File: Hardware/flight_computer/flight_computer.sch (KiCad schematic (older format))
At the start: 38 parts, among them J1 Micro_USB, J2 MicroSD_molex, J3 rpi_zero_w, Q1 PMOS_20V_.76A, Q2 PMOS_20V_.76A, U1 FRAM_128K, U2 STM32F427VITx, U3 MCP131T-300E_TT, Y1 Crystal_24MHZ

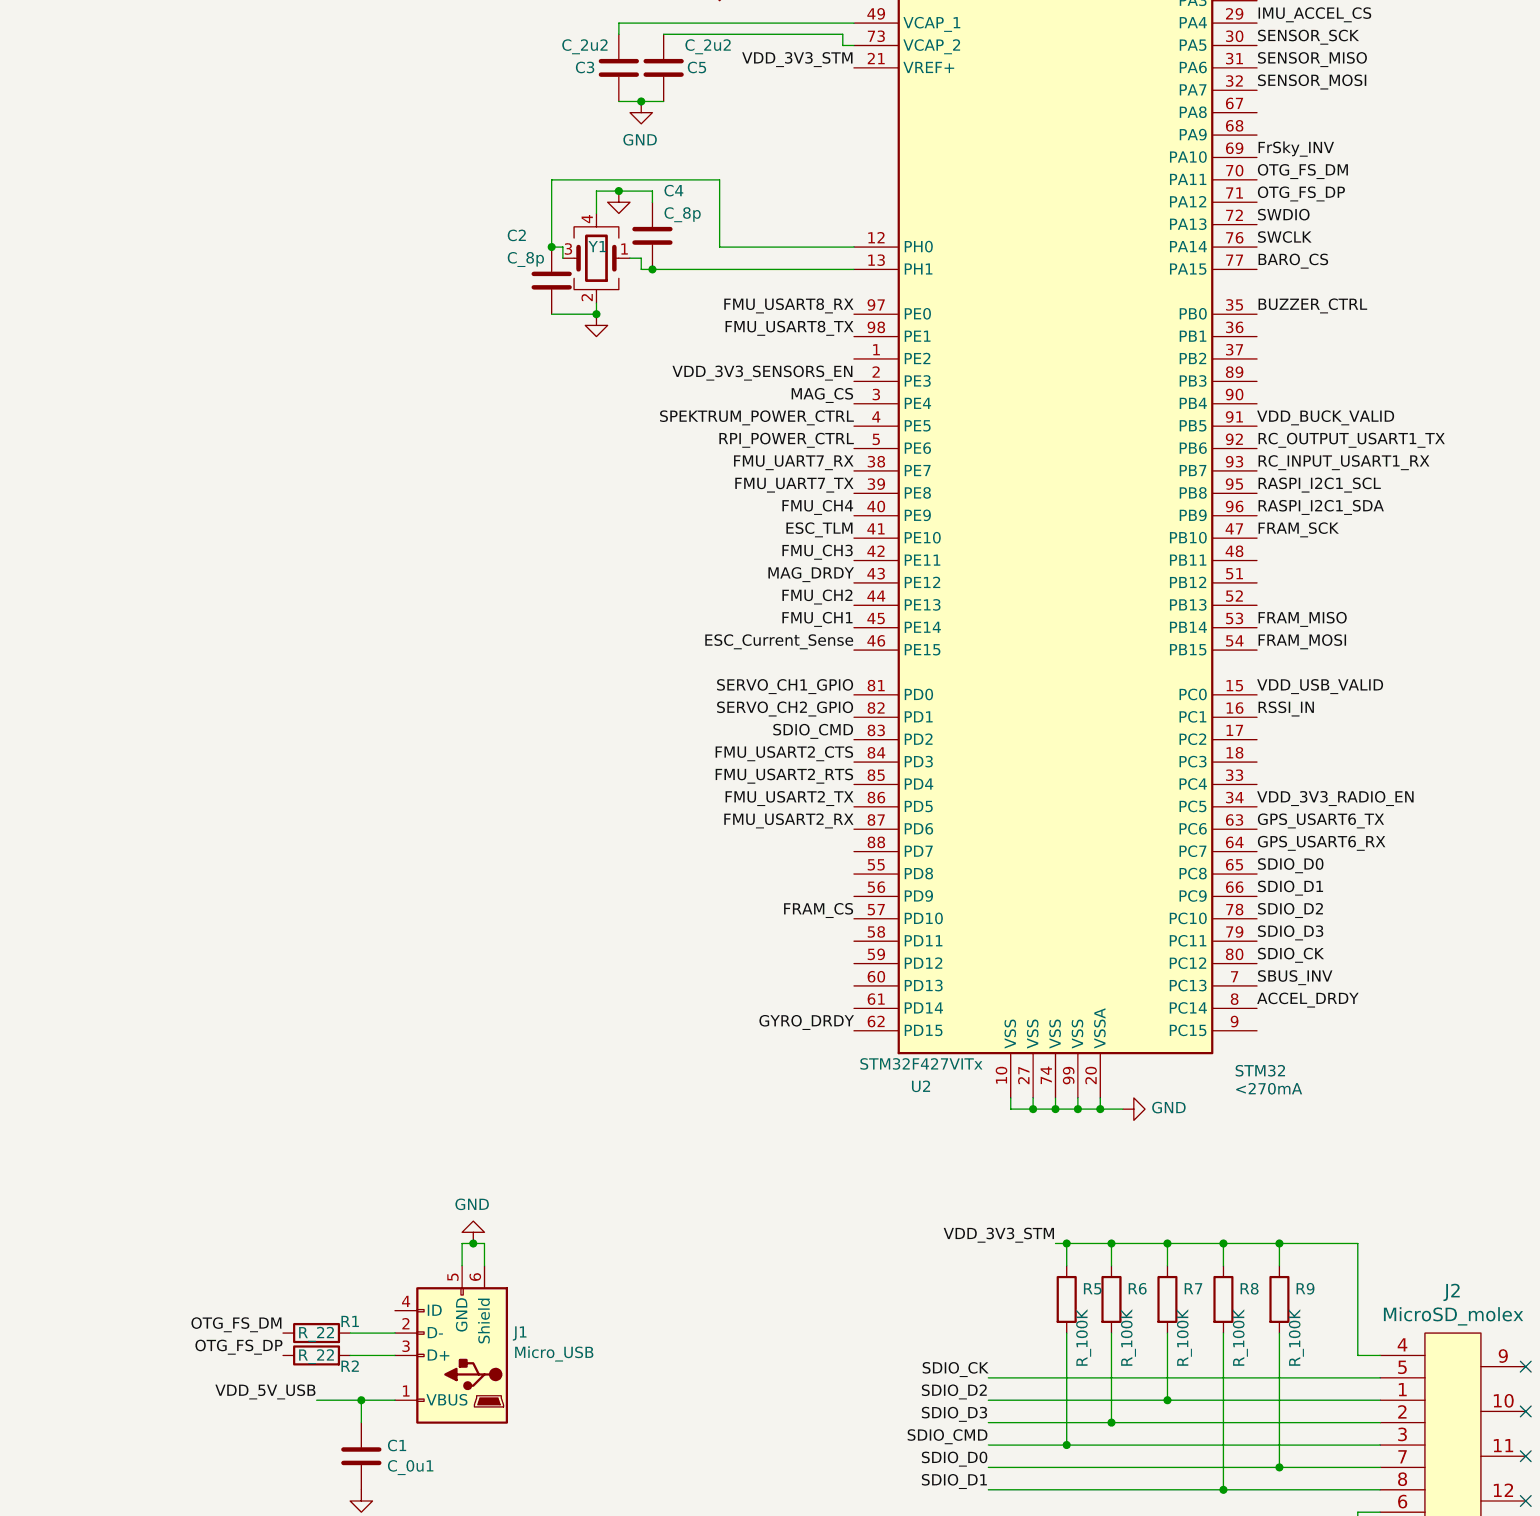
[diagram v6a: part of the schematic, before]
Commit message: started buck layout
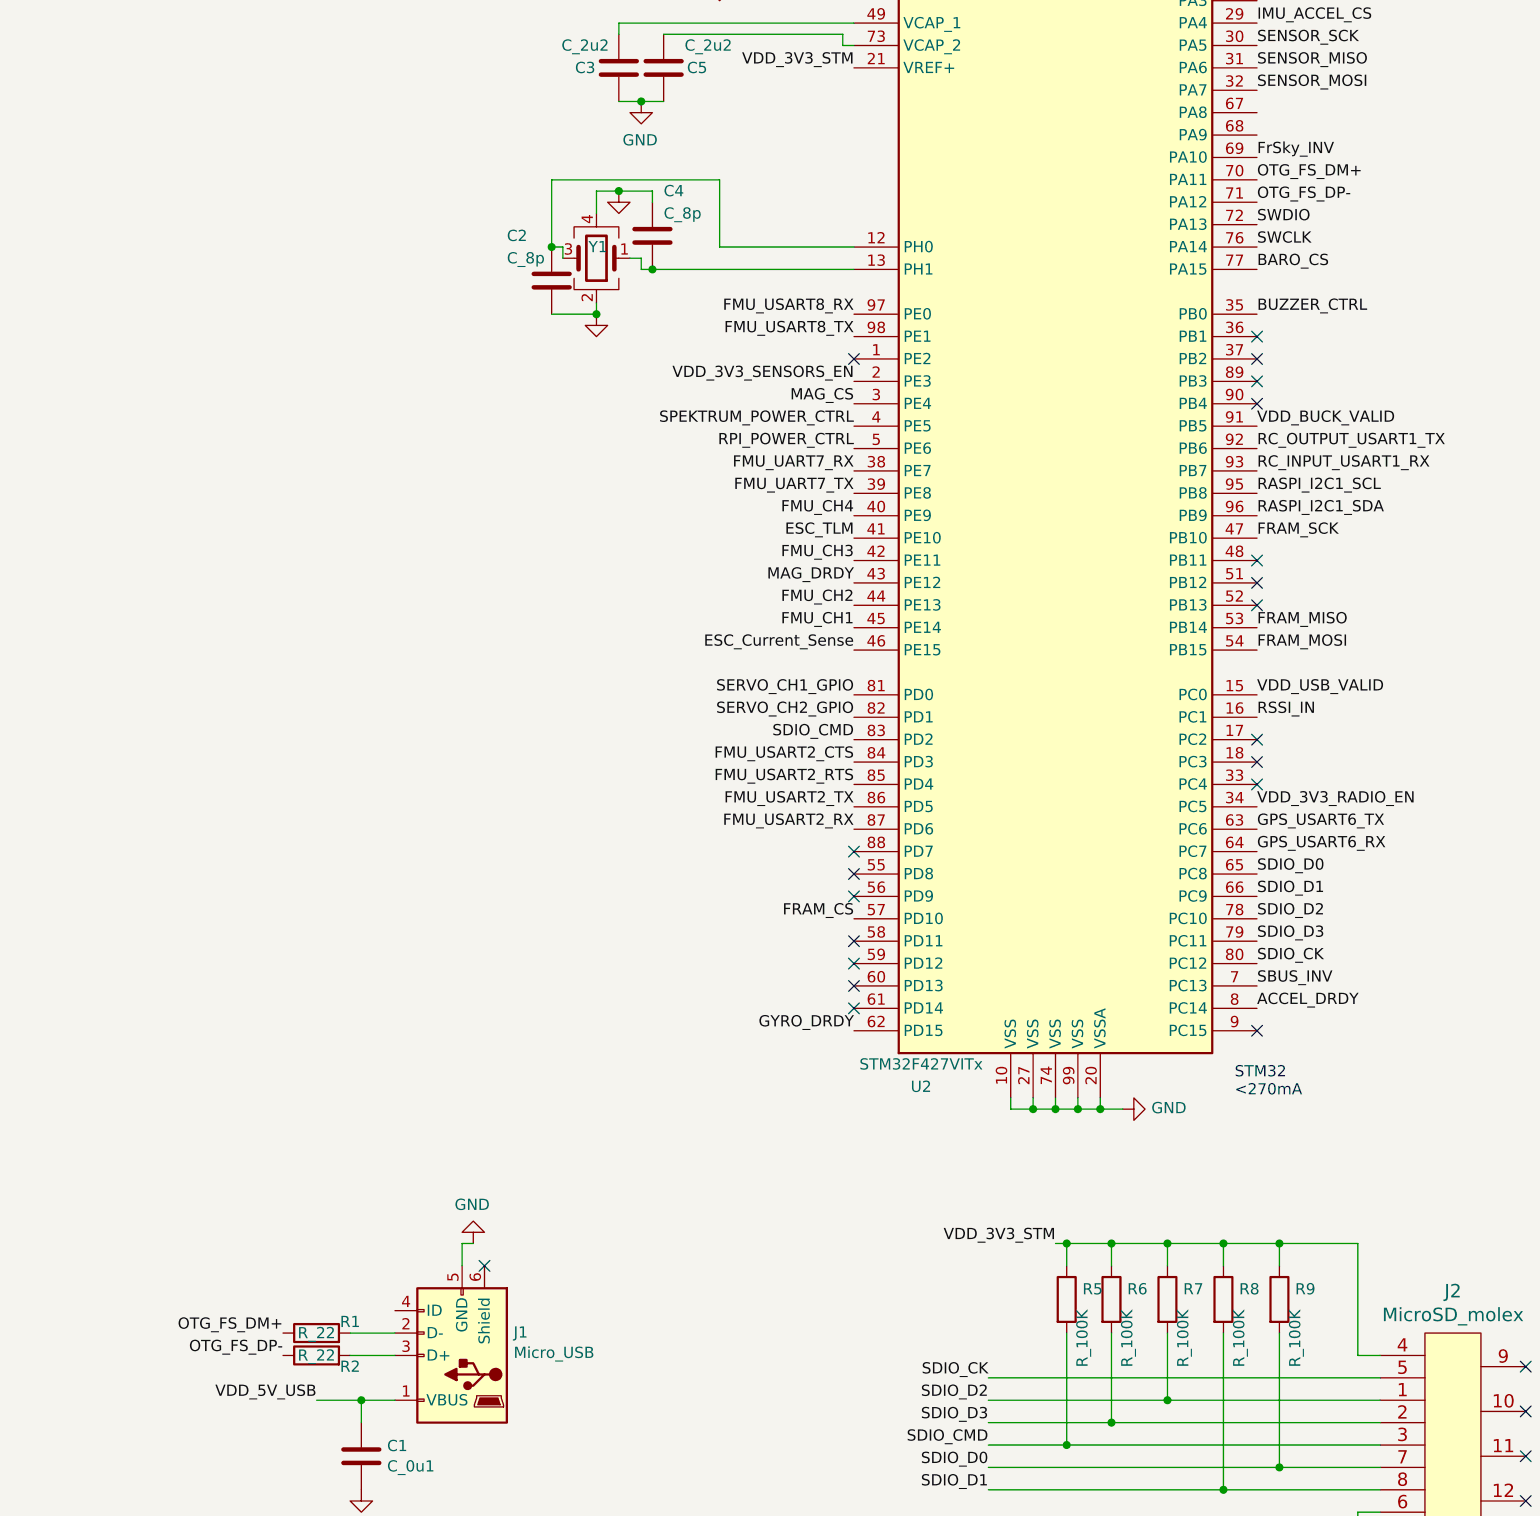
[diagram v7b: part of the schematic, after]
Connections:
- net GND: no longer J1.6 (Shield)
- net OTG_FS_DM renamed OTG_FS_DM+
- net OTG_FS_DP renamed OTG_FS_DP-
- no-connect marks 4 -> 24
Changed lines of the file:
@@
 	7450 1900 7450 1800
 Wire Wire Line
-	7750 2000 7750 1850
-Wire Wire Line
 	7750 1850 7650 1850
 Wire Wire Line
 	7650 1850 7650 1800
 Wire Wire Line
-	7850 2000 7850 1800
-Wire Wire Line
-	7950 2000 7950 1800
-Wire Wire Line
 	7950 1800 8050 1800
-Wire Wire Line
-	8050 2000 8050 1850
 Wire Wire Line
 	8050 1850 8250 1850
@@
 Text Label 6950 6200 2    50   ~ 0
 FMU_USART2_TX
-$Comp
-L MCU_ST_STM32F4:STM32F427VITx U2
-U 1 1 5F5EC592
-P 7850 4700
-F 0 "U2" H 7250 1950 50  0000 C CNN
-F 1 "STM32F427VITx" H 7250 2050 50  0000 C CNN
-F 2 "drone_footprints:QFP50P1600X1600X160-100N" H 7150 2100 50  0001 R CNN
-F 3 "http://www.st.com/st-web-ui/static/active/en/resource/technical/document/datasheet/DM00071990.pdf" H 7850 4700 50  0001 C CNN
-	1    7850 4700
-	1    0    0    -1
-$EndComp
 Text Label 6950 6300 2    50   ~ 0
 FMU_USART2_RX
@@
 GPS_USART6_RX
 Text Label 8750 3400 0    50   ~ 0
-OTG_FS_DM
-Text Label 8750 3500 0    50   ~ 0
-OTG_FS_DP
+OTG_FS_DM+
 Text Label 8750 3600 0    50   ~ 0
 SWDIO
@@
 $EndComp
 Wire Wire Line
-	5300 8250 5300 8150
-Wire Wire Line
-	5300 8150 5250 8150
-Wire Wire Line
 	5200 8250 5200 8150
 Wire Wire Line
 	5200 8150 5250 8150
-Connection ~ 5250 8150
 Text Label 4400 8550 2    50   ~ 0
-OTG_FS_DM
+OTG_FS_DM+
 Text Label 4400 8650 2    50   ~ 0
-OTG_FS_DP
+OTG_FS_DP-
 Text Label 4550 8850 2    50   ~ 0
 VDD_5V_USB
@@
 Text Label 1700 1300 0    50   ~ 0
 ESC_TLM
+Wire Wire Line
+	8050 2000 8050 1850
+Wire Wire Line
+	7950 2000 7950 1800
+Wire Wire Line
+	7850 2000 7850 1800
+Wire Wire Line
+	7750 2000 7750 1850
+$Comp
+L MCU_ST_STM32F4:STM32F427VITx U2
+U 1 1 5F5EC592
+P 7850 4700
+F 0 "U2" H 7250 1950 50  0000 C CNN
+F 1 "STM32F427VITx" H 7250 2050 50  0000 C CNN
+F 2 "drone_footprints:QFP50P1600X1600X160-100N" H 7150 2100 50  0001 R CNN
+F 3 "http://www.st.com/st-web-ui/static/active/en/resource/technical/document/datasheet/DM00071990.pdf" H 7850 4700 50  0001 C CNN
+	1    7850 4700
+	1    0    0    -1
+$EndComp
+NoConn ~ 8750 7200
+NoConn ~ 8750 5900
+NoConn ~ 8750 6000
+NoConn ~ 8750 6100
+NoConn ~ 8750 5100
+NoConn ~ 8750 5200
+NoConn ~ 8750 5300
+NoConn ~ 8750 4100
+NoConn ~ 8750 4200
+NoConn ~ 8750 4300
+NoConn ~ 8750 4400
+NoConn ~ 6950 6400
+NoConn ~ 6950 6500
+NoConn ~ 6950 6600
+NoConn ~ 6950 6800
+NoConn ~ 6950 6900
+NoConn ~ 6950 7000
+NoConn ~ 6950 7100
+NoConn ~ 6950 4200
+NoConn ~ 5300 8250
+Text Label 8750 3500 0    50   ~ 0
+OTG_FS_DP-
 $EndSCHEMATC

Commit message: worked on layout
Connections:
- net OTG_FS_DM+ renamed OTG_FS_D_N
- net OTG_FS_DP- renamed OTG_FS_D_P
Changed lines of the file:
@@
 GPS_USART6_RX
 Text Label 8750 3400 0    50   ~ 0
-OTG_FS_DM+
+OTG_FS_D_N
 Text Label 8750 3600 0    50   ~ 0
 SWDIO
@@
 Wire Wire Line
 	5200 8150 5250 8150
-Text Label 4400 8550 2    50   ~ 0
-OTG_FS_DM+
-Text Label 4400 8650 2    50   ~ 0
-OTG_FS_DP-
 Text Label 4550 8850 2    50   ~ 0
 VDD_5V_USB
@@
 NoConn ~ 5300 8250
 Text Label 8750 3500 0    50   ~ 0
-OTG_FS_DP-
+OTG_FS_D_P
+Text Label 4400 8650 2    50   ~ 0
+OTG_FS_D_P
+Text Label 4400 8550 2    50   ~ 0
+OTG_FS_D_N
 $EndSCHEMATC
